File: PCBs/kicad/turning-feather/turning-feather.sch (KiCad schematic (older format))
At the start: 21 parts, among them J1 Out to RJ45, J2 Buttons/beep, J3 Off switch, U1 TSR 1-2450, U2 MIC4427, U3 MIC4427, U4 ZPT

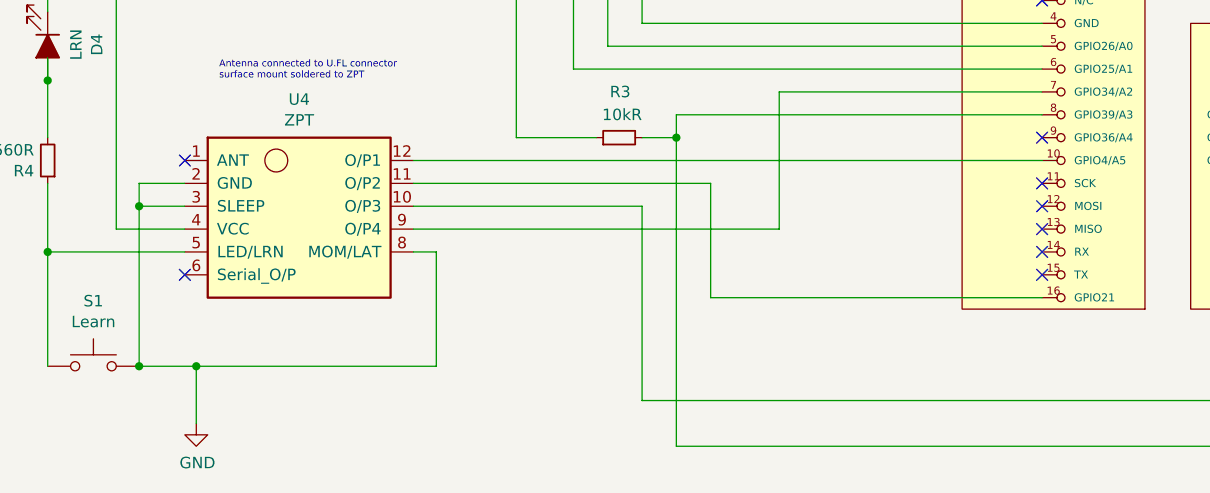
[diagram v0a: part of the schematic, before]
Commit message: Add serial output from ZPT to serial in on feather. PCB V0.23.
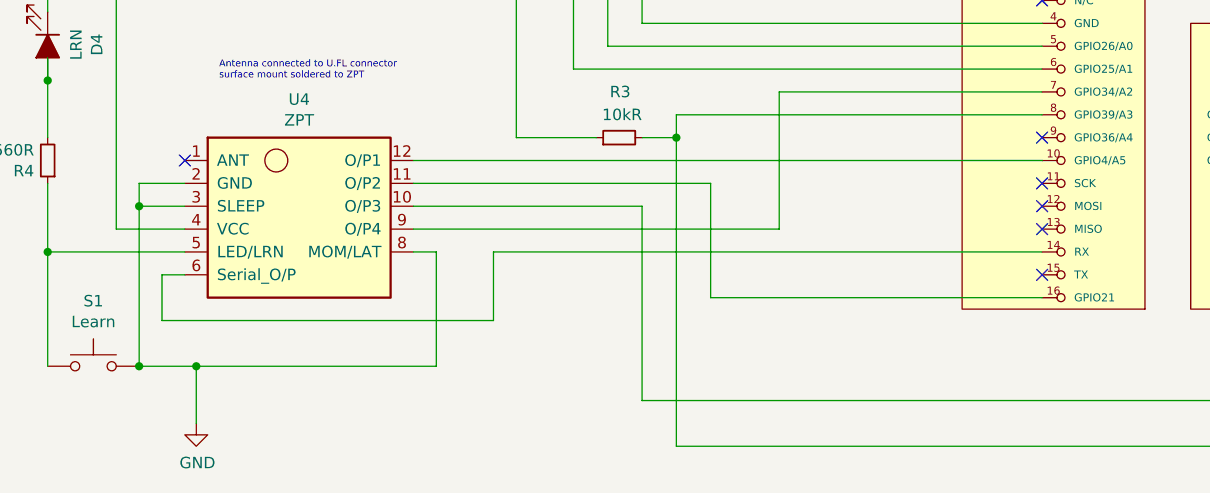
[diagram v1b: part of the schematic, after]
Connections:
- net at U4.6 (Serial_O/P): now also JP1.14 (RX)
- no-connect marks 20 -> 18
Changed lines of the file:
@@
 NoConn ~ 9950 4750
 NoConn ~ 1650 4350
-NoConn ~ 1650 4850
 Wire Wire Line
 	1450 4550 1450 5250
@@
 NoConn ~ 6550 4950
 NoConn ~ 5400 4850
-NoConn ~ 5400 4750
 NoConn ~ 5400 4650
 NoConn ~ 5400 4550
@@
 Text Notes 1800 4000 0    30   ~ 0
 Antenna connected to U.FL connector\nsurface mount soldered to ZPT
+Wire Wire Line
+	5400 4750 3000 4750
+Wire Wire Line
+	3000 4750 3000 5050
+Wire Wire Line
+	3000 5050 1550 5050
+Wire Wire Line
+	1550 5050 1550 4850
+Wire Wire Line
+	1550 4850 1650 4850
 $EndSCHEMATC

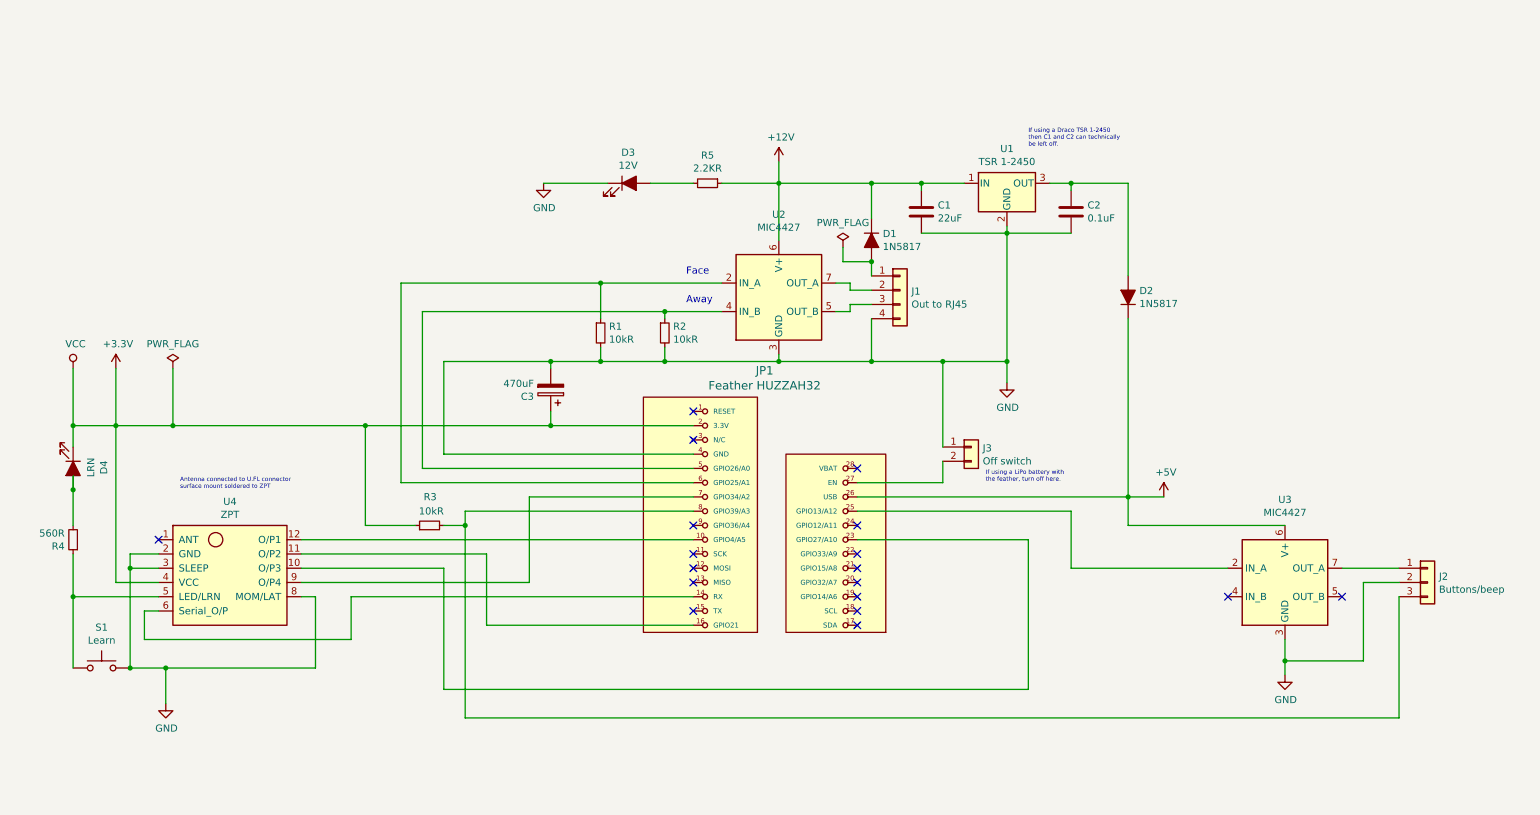
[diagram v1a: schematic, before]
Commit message: PCB version 0.32.
Add serial connection from ZPT to Serial2 on HUZZAH32.
Connect spare 5V MOSFET input to spare HUZZAH32 output with header.
Add on-board PCB mount RJ45 as an option, old connector retained.
Move LEDs out to new board extension back to point towards user.
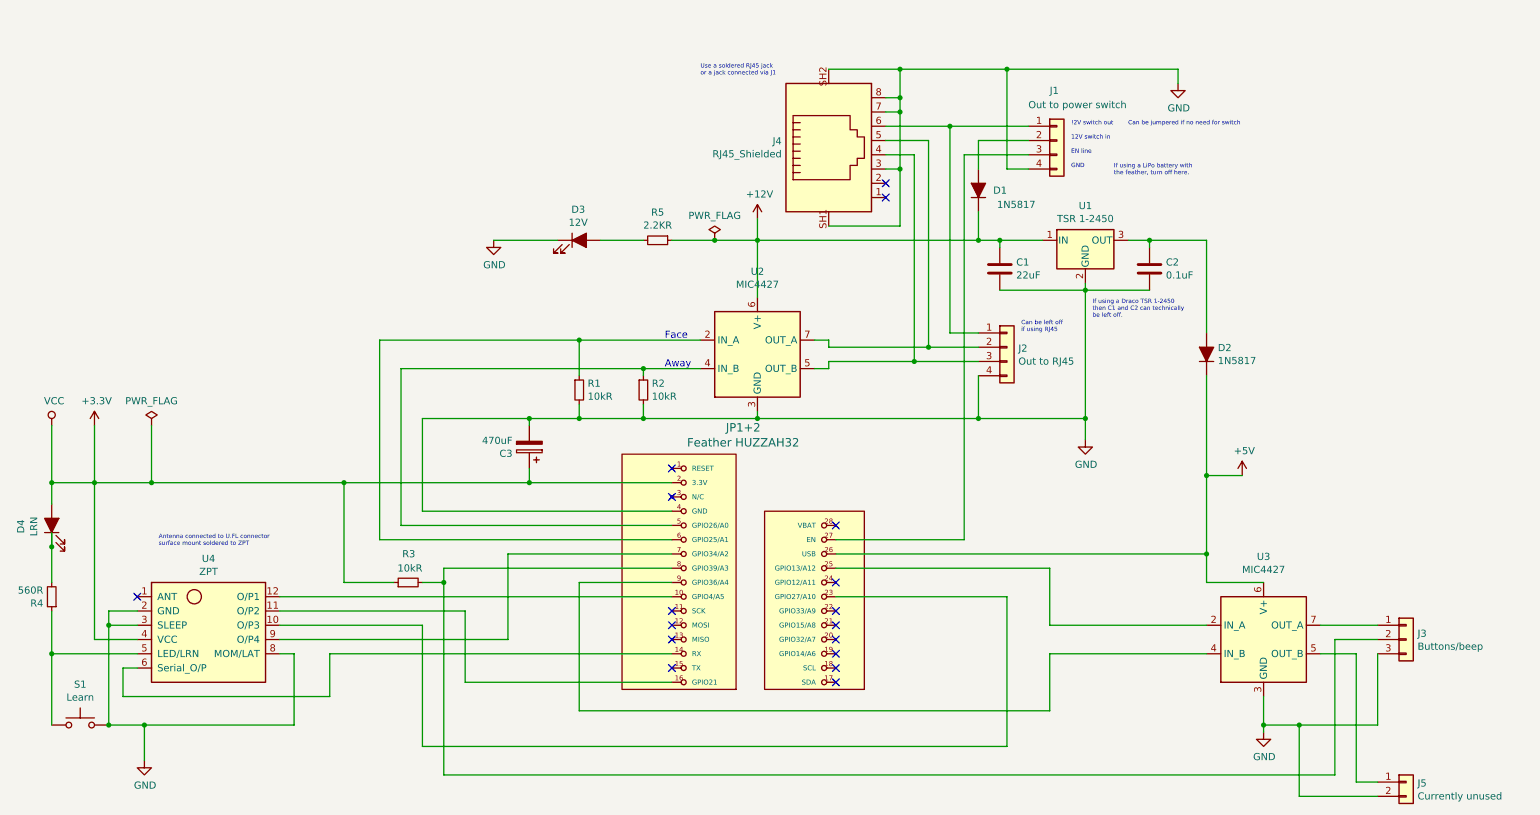
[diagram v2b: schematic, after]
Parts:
- removed J3: Off switch, Connector_JST:JST_PH_S2B-PH-K_1x02_P2.00mm_Horizontal, symbol Connector_Generic:Conn_01x02
- added J1: Out to power switch, Connector_JST:JST_PH_S4B-PH-K_1x04_P2.00mm_Horizontal, symbol Connector_Generic:Conn_01x04
- added J4: RJ45_Shielded, turning-feather:RJ45_Horizontal_Shielded, symbol feather:8P8C_Shielded
- added J5: Currently unused, Connector_JST:JST_PH_S2B-PH-K_1x02_P2.00mm_Horizontal, symbol Connector_Generic:Conn_01x02
- C3: footprint Capacitor_THT:CP_Radial_D8.0mm_P5.00mm -> Capacitor_THT:CP_Radial_D6.3mm_P2.50mm
- renumbered J1 to J2, J2 to J3, JP1 to JP1+2
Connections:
- net +3V3: now also D4.2 (A); no longer D4.1 (K)
- net GND: now also J3.3 (Pin_3), J1.4 (Pin_4), J4.3, J4.7, J4.8, J4.SH1, J4.SH2, J5.2 (Pin_2); no longer J3.2 (Pin_2)
- net at J2.1 (Pin_1): now also J1.1 (Pin_1), J4.6; no longer D1.2 (A)
- net at J2.2 (Pin_2), U2.7 (OUT_A): now also J4.5
- net at J2.3 (Pin_3), U2.5 (OUT_B): now also J4.4
- net at JP1+2.8 (GPIO39/A3), R3.2: now also J3.2 (Pin_2); no longer J3.3 (Pin_3)
- net at R4.2: now also D4.1 (K); no longer D4.2 (A)
- net at JP1+2.27 (EN): now also J1.3 (Pin_3)
- net at JP1+2.9 (GPIO36/A4): now also U3.4 (IN_B)
- net at U3.5 (OUT_B): now also J5.1 (Pin_1)
- new net: D1.2 (A), J1.2 (Pin_2)
- no-connect marks 18 -> 17
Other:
- note added: "!2V switch out"
- note added: "12V switch in"
- note added: "Can be jumpered if no need for switch"
- note added: "Can be left off\nif using RJ45"
- note added: "EN line"
- note added: "GND"
- note added: "Use a soldered RJ45 jack\nor a jack connected via J1"
- moved on the sheet: C1, C2, C3, D1, D2, D3, D4, J2, J3, JP1+2, R1, R2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

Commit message: Move ethernet on-PCB, move most things around, change capacitors, etc
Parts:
- removed J5: Currently unused, Connector_JST:JST_PH_S2B-PH-K_1x02_P2.00mm_Horizontal, symbol Connector_Generic:Conn_01x02
- added D3: 1N5817, Diode_THT:D_DO-41_SOD81_P10.16mm_Horizontal, symbol Diode:1N5817
- added J5: Spare, Connector_PinHeader_1.00mm:PinHeader_1x01_P1.00mm_Vertical, symbol Connector_Generic:Conn_01x01
- C1: footprint Capacitor_THT:C_Disc_D7.5mm_W2.5mm_P5.00mm -> Capacitor_THT:CP_Radial_Tantal_D4.5mm_P2.50mm
- D1, D2: footprint Diode_THT:D_A-405_P7.62mm_Horizontal -> Diode_THT:D_DO-41_SOD81_P10.16mm_Horizontal; symbol Device:D_ALT -> Diode:1N5817
- renumbered D3 to D5
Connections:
- net +12V: now also R5.2, D3.2 (A); no longer R5.1, U2.6 (V+)
- net at U3.5 (OUT_B): now also J5.1 (Pin_1)
- net at JP1+2.24 (GPIO12/A11): now also U3.4 (IN_B)
- net at JP1+2.9 (GPIO36/A4): no longer U3.4 (IN_B)
- net at D5.2 (A): now also R5.1; no longer R5.2
- new net: D3.1 (K), U2.6 (V+)
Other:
- moved on the sheet: D5, J1, J4, R5

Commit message: Some cleanup to pcb and schema
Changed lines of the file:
@@
 Text Notes 8200 2800 0    30   ~ 0
 If using a Draco TSR 1-2450\nthen C1 and C2 can technically\nbe left off.
-Text Notes 8350 1450 0    30   ~ 0
+Text Notes 8300 1400 0    30   ~ 0
 If using a LiPo battery with\nthe feather, turn off here.
 Text Notes 1650 4400 0    30   ~ 0
